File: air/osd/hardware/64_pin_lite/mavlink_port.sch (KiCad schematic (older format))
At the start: 4 parts, among them P4 CONN_6, U6 SI8642

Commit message: osd first  no eror routing of pcb
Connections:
- net FC_FRSKY_RXI: no longer P4.1, U6.14 (B1)
- new net FC_FRSKY_TXO: P4.1, U6.14 (B1)
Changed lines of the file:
@@
-EESchema Schematic File Version 2  date Thu 27 Nov 2014 15:59:43 GMT
+EESchema Schematic File Version 2  date Sat 29 Nov 2014 10:43:44 GMT
 LIBS:power
 LIBS:device
@@
 Sheet 6 8
 Title ""
-Date "27 nov 2014"
+Date "29 nov 2014"
 Rev ""
 Comp ""
@@
 $EndComp
 Text Label 7100 3800 0    45   ~ 0
-FC_FRSKY_RXI
+FC_FRSKY_TXO
 Text Label 7100 3700 0    45   ~ 0
 FC_GND

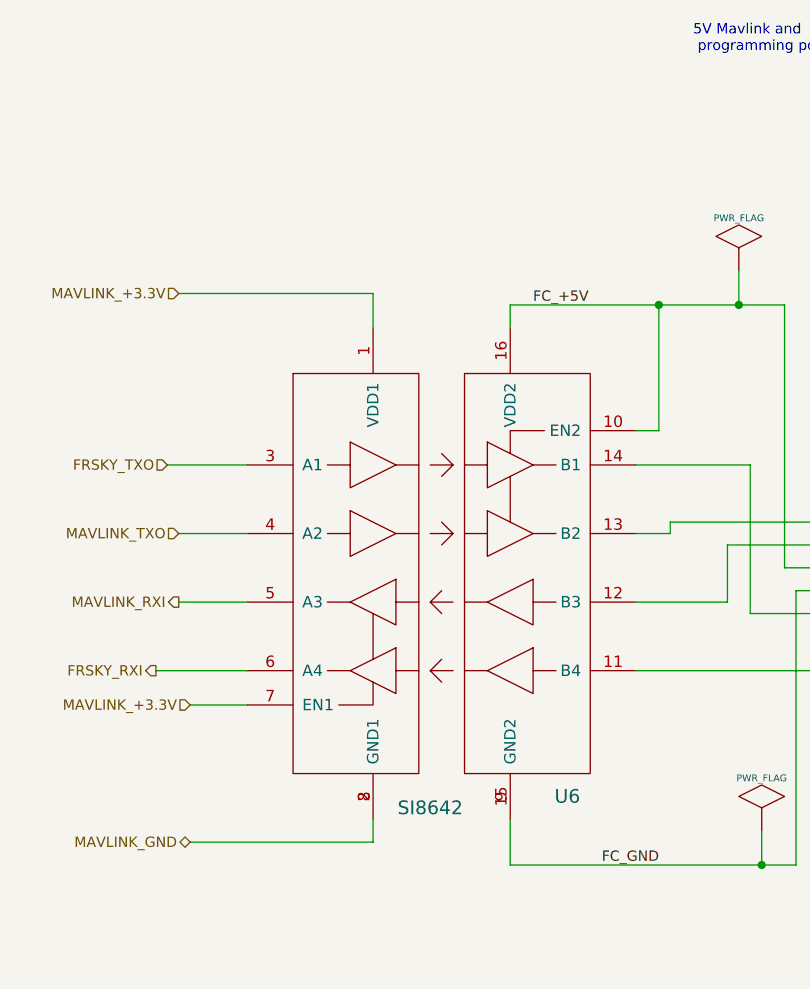
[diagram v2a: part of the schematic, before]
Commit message: added links for isolted port and other mods
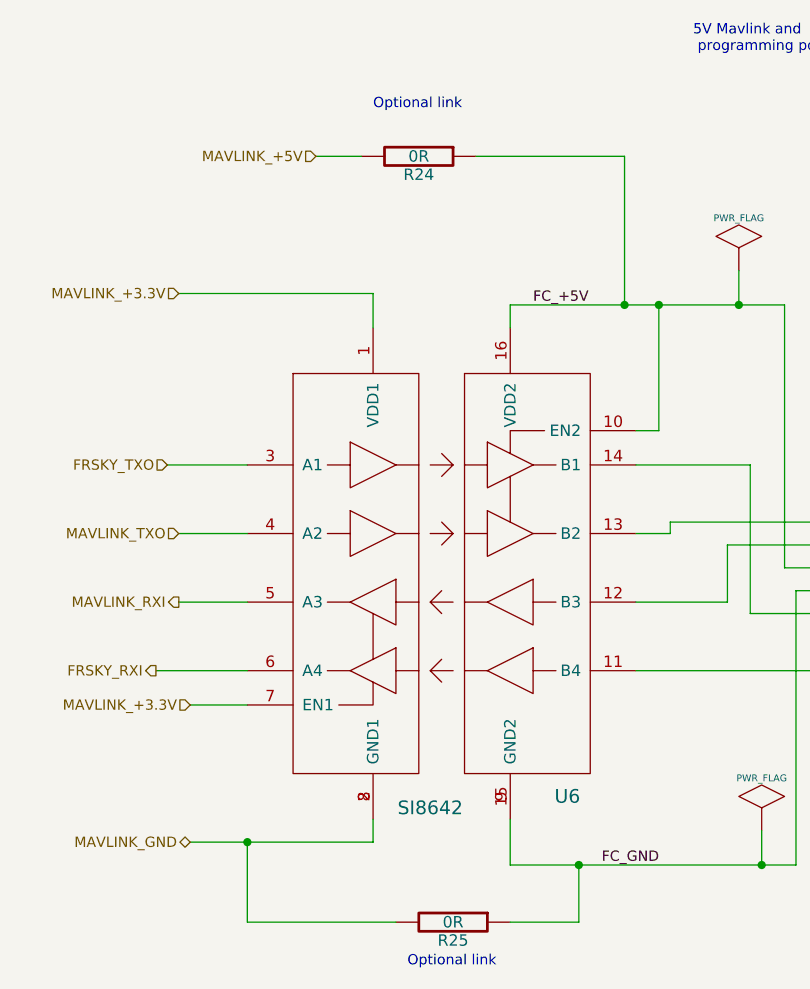
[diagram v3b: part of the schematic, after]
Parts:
- added R24, R25: 0R, symbol R
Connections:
- net FC_+5V: now also R24.1
- net FC_GND: now also R25.1
- net MAVLINK_GND: now also R25.2
- new net MAVLINK_+5V: R24.2
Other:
- note added: "Optional link"
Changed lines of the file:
@@
-EESchema Schematic File Version 2  date Sun 30 Nov 2014 15:34:12 GMT
+EESchema Schematic File Version 2  date Mon 01 Dec 2014 08:28:41 GMT
 LIBS:power
 LIBS:device
@@
 Sheet 6 8
 Title ""
-Date "30 nov 2014"
+Date "1 dec 2014"
 Rev ""
 Comp ""
@@
 Comment4 ""
 $EndDescr
+Text Notes 5100 1600 0    45   ~ 0
+Optional link
+Text Notes 5250 5350 0    45   ~ 0
+Optional link
+Connection ~ 4550 4800
+Wire Wire Line
+	4550 4800 4550 5150
+Wire Wire Line
+	4550 5150 5200 5150
+Connection ~ 6200 2450
+Wire Wire Line
+	6200 2450 6200 1800
+Wire Wire Line
+	6200 1800 5550 1800
 Wire Wire Line
 	2700 2800 2800 2800
@@
 Wire Wire Line
 	2800 2250 2800 2350
+Wire Wire Line
+	5050 1800 4850 1800
+Wire Wire Line
+	5700 5150 6000 5150
+Wire Wire Line
+	6000 5150 6000 4900
+Connection ~ 6000 4900
+$Comp
+L R R25
+U 1 1 547C2609
+P 5450 5150
+F 0 "R25" V 5530 5150 50  0000 C CNN
+F 1 "0R" V 5450 5150 50  0000 C CNN
+	1    5450 5150
+	0    1    1    0
+$EndComp
+$Comp
+L R R24
+U 1 1 547C2601
+P 5300 1800
+F 0 "R24" V 5380 1800 50  0000 C CNN
+F 1 "0R" V 5300 1800 50  0000 C CNN
+	1    5300 1800
+	0    1    1    0
+$EndComp
+Text HLabel 4850 1800 0    45   Input ~ 0
+MAVLINK_+5V
 Text HLabel 2700 2800 0    45   BiDi ~ 0
 MAVLINK_GND
@@
 FC_GND
 $Comp
-L PWR_FLAG #FLG05
+L PWR_FLAG #FLG6
 U 1 1 547339AD
 P 6800 4750
-F 0 "#FLG05" H 6800 5020 30  0001 C CNN
+F 0 "#FLG6" H 6800 5020 30  0001 C CNN
 F 1 "PWR_FLAG" H 6800 4980 30  0000 C CNN
 	1    6800 4750
@@
 $EndComp
 $Comp
-L PWR_FLAG #FLG06
+L PWR_FLAG #FLG5
 U 1 1 547339A4
 P 6700 2300
-F 0 "#FLG06" H 6700 2570 30  0001 C CNN
+F 0 "#FLG5" H 6700 2570 30  0001 C CNN
 F 1 "PWR_FLAG" H 6700 2530 30  0000 C CNN
 	1    6700 2300

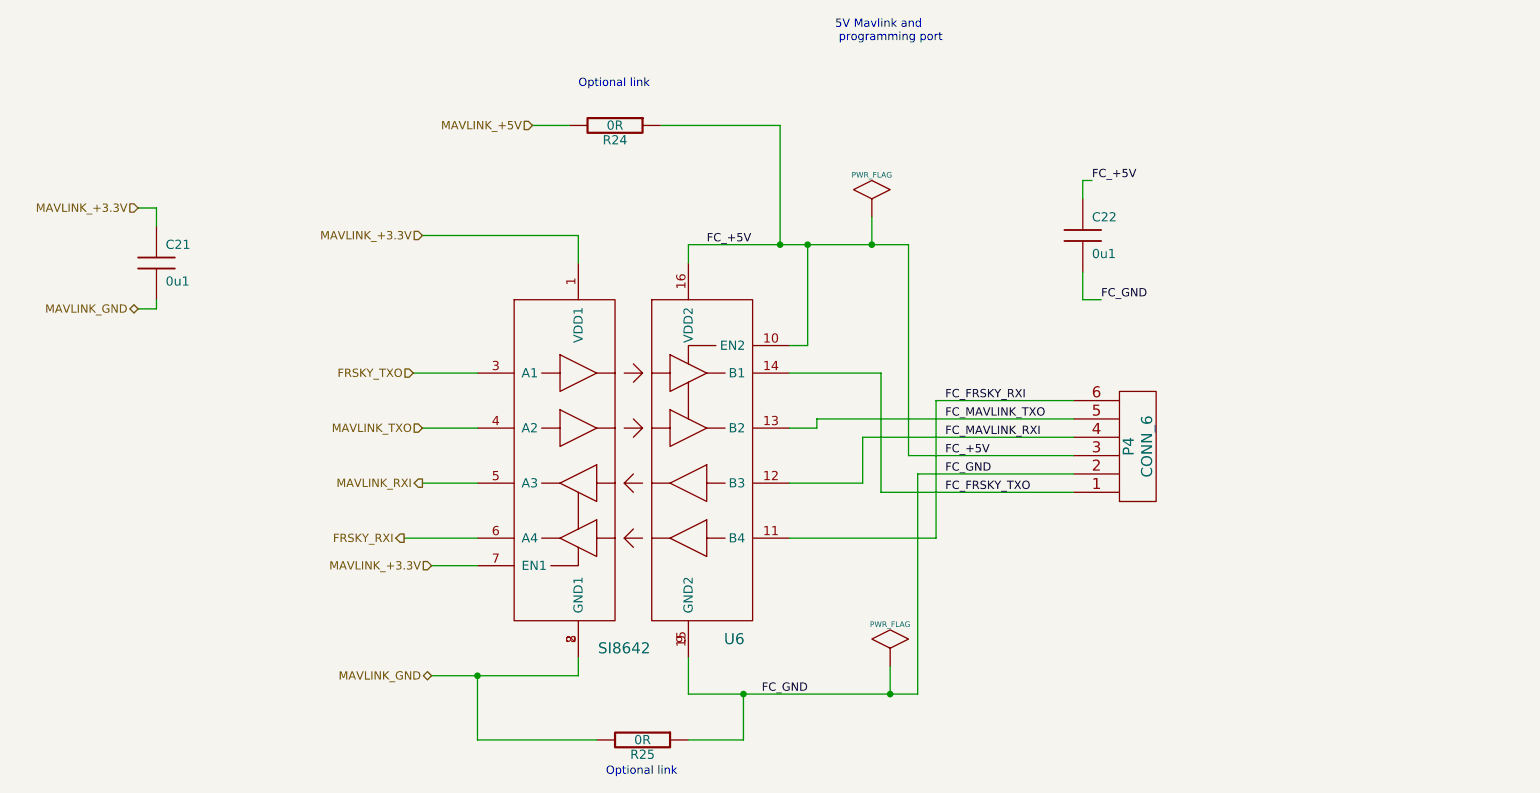
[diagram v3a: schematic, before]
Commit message: added resistors to output port on board and satrted on boardtype 4 port but currently in transition
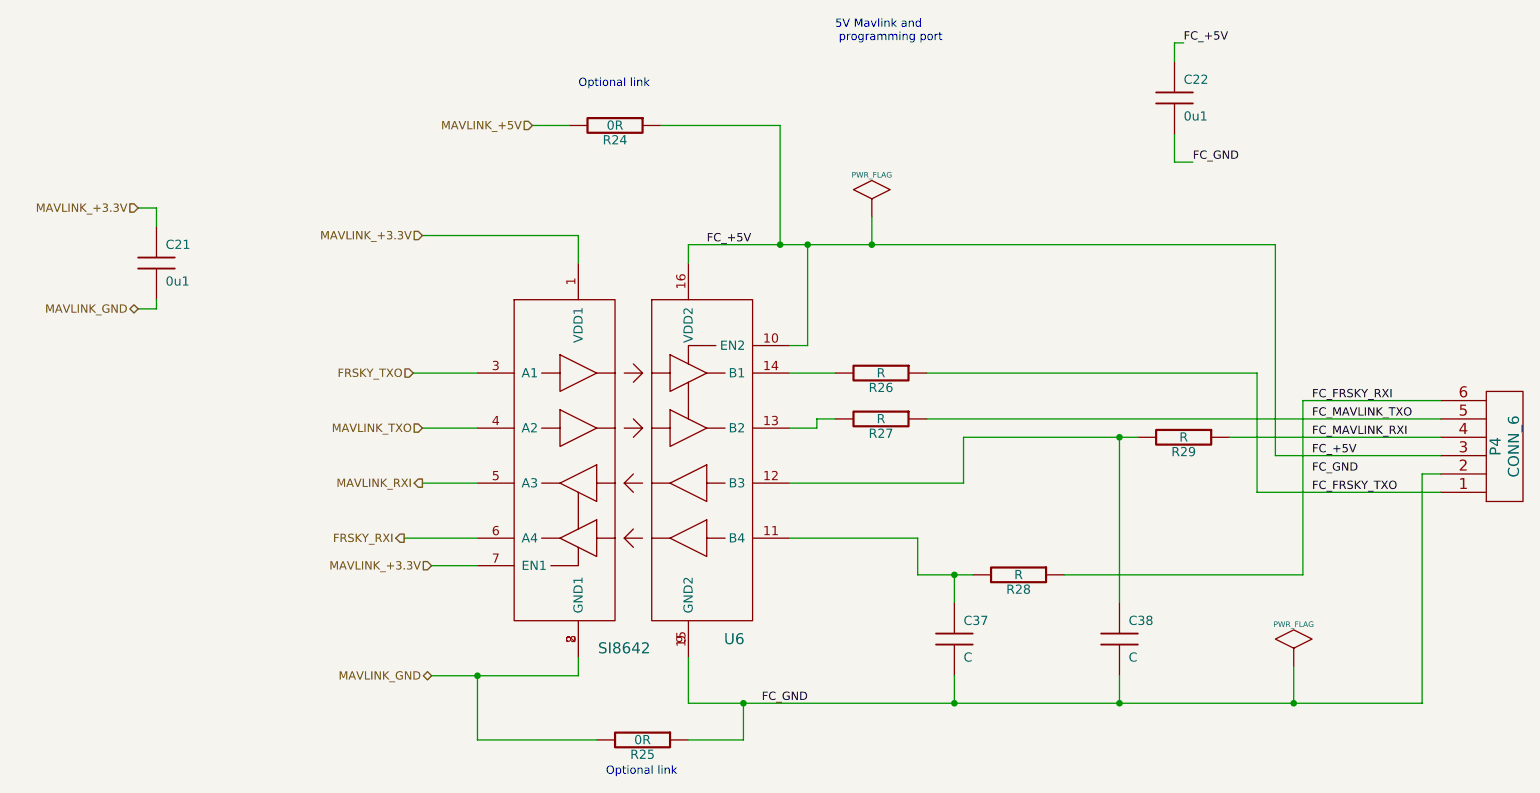
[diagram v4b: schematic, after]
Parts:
- added C37, C38: C, symbol C
- added R26, R27, R28, R29: R, symbol R
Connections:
- net FC_FRSKY_RXI: now also R28.1; no longer U6.11 (B4)
- net FC_FRSKY_TXO: now also R26.1; no longer U6.14 (B1)
- net FC_GND: now also C37.2, C38.2
- net FC_MAVLINK_RXI: now also R29.1; no longer U6.12 (B3)
- net FC_MAVLINK_TXO: now also R27.1; no longer U6.13 (B2)
- new net: C37.1, R28.2, U6.11 (B4)
- new net: C38.1, R29.2, U6.12 (B3)
- new net: R27.2, U6.13 (B2)
- new net: R26.2, U6.14 (B1)
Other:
- moved on the sheet: C22, P4
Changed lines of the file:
@@
-EESchema Schematic File Version 2  date Mon 01 Dec 2014 08:28:41 GMT
+EESchema Schematic File Version 2  date Tue 02 Dec 2014 12:33:05 GMT
 LIBS:power
 LIBS:device
@@
 Sheet 6 8
 Title ""
-Date "1 dec 2014"
+Date "2 dec 2014"
 Rev ""
 Comp ""
@@
 Comment4 ""
 $EndDescr
+Connection ~ 7150 4950
+Wire Wire Line
+	7150 4950 7150 4800
+Connection ~ 8050 3500
+Wire Wire Line
+	8050 4400 8050 3500
+Connection ~ 4550 4800
+Wire Wire Line
+	4550 4800 4550 5150
+Wire Wire Line
+	4550 5150 5200 5150
+Connection ~ 6200 2450
+Wire Wire Line
+	6200 2450 6200 1800
+Wire Wire Line
+	6200 1800 5550 1800
+Wire Wire Line
+	2700 2800 2800 2800
+Wire Wire Line
+	2800 2800 2800 2750
+Wire Wire Line
+	8350 1850 8350 2000
+Wire Wire Line
+	8350 2000 8450 2000
+Wire Wire Line
+	4550 4050 4150 4050
+Wire Wire Line
+	5100 4700 5100 4800
+Wire Wire Line
+	5100 4800 4300 4800
+Connection ~ 9000 4950
+Wire Wire Line
+	9000 4750 9000 4950
+Wire Wire Line
+	4550 3750 4250 3750
+Wire Wire Line
+	4550 3150 4200 3150
+Wire Wire Line
+	9050 3300 9050 4250
+Wire Wire Line
+	9050 3300 9800 3300
+Wire Wire Line
+	7250 4250 6950 4250
+Wire Wire Line
+	6950 4250 6950 4050
+Wire Wire Line
+	6950 4050 6250 4050
+Wire Wire Line
+	9050 4250 7750 4250
+Wire Wire Line
+	7000 3150 8800 3150
+Wire Wire Line
+	6250 3150 6500 3150
+Wire Wire Line
+	5100 2550 5100 2400
+Wire Wire Line
+	5100 2400 4250 2400
+Wire Wire Line
+	9800 3700 9700 3700
+Wire Wire Line
+	9700 3700 9700 4950
+Wire Wire Line
+	9700 4950 5700 4950
+Wire Wire Line
+	5700 4950 5700 4700
+Wire Wire Line
+	5700 2550 5700 2450
+Wire Wire Line
+	5700 2450 8900 2450
+Wire Wire Line
+	8900 2450 8900 3600
+Wire Wire Line
+	8900 3600 9800 3600
+Wire Wire Line
+	6250 3000 6350 3000
+Wire Wire Line
+	6350 3000 6350 2450
+Connection ~ 6350 2450
+Wire Wire Line
+	4550 4200 4300 4200
+Wire Wire Line
+	8150 3500 7200 3500
+Wire Wire Line
+	9800 3500 8650 3500
+Wire Wire Line
+	7200 3500 7200 3750
+Wire Wire Line
+	7200 3750 6250 3750
+Wire Wire Line
+	6500 3400 6400 3400
+Wire Wire Line
+	9800 3400 7000 3400
+Wire Wire Line
+	6400 3400 6400 3450
+Wire Wire Line
+	6400 3450 6250 3450
+Wire Wire Line
+	9800 3800 8800 3800
+Wire Wire Line
+	8800 3800 8800 3150
+Wire Wire Line
+	4550 3450 4250 3450
+Wire Wire Line
+	6700 2300 6700 2450
+Connection ~ 6700 2450
+Wire Wire Line
+	8350 1450 8350 1350
+Wire Wire Line
+	8350 1350 8400 1350
+Wire Wire Line
+	2700 2250 2800 2250
+Wire Wire Line
+	2800 2250 2800 2350
+Wire Wire Line
+	5050 1800 4850 1800
+Wire Wire Line
+	5700 5150 6000 5150
+Wire Wire Line
+	6000 5150 6000 4950
+Connection ~ 6000 4950
+Wire Wire Line
+	8050 4800 8050 4950
+Connection ~ 8050 4950
+Wire Wire Line
+	7150 4400 7150 4250
+Connection ~ 7150 4250
+$Comp
+L C C37
+U 1 1 547D825F
+P 7150 4600
+F 0 "C37" H 7200 4700 50  0000 L CNN
+F 1 "C" H 7200 4500 50  0000 L CNN
+	1    7150 4600
+	1    0    0    -1
+$EndComp
+$Comp
+L C C38
+U 1 1 547D8257
+P 8050 4600
+F 0 "C38" H 8100 4700 50  0000 L CNN
+F 1 "C" H 8100 4500 50  0000 L CNN
+	1    8050 4600
+	1    0    0    -1
+$EndComp
+$Comp
+L R R29
+U 1 1 547D81DE
+P 8400 3500
+F 0 "R29" V 8480 3500 50  0000 C CNN
+F 1 "R" V 8400 3500 50  0000 C CNN
+	1    8400 3500
+	0    1    1    0
+$EndComp
+$Comp
+L R R28
+U 1 1 547D81C5
+P 7500 4250
+F 0 "R28" V 7580 4250 50  0000 C CNN
+F 1 "R" V 7500 4250 50  0000 C CNN
+	1    7500 4250
+	0    1    1    0
+$EndComp
+$Comp
+L R R27
+U 1 1 547D816E
+P 6750 3400
+F 0 "R27" V 6830 3400 50  0000 C CNN
+F 1 "R" V 6750 3400 50  0000 C CNN
+	1    6750 3400
+	0    1    1    0
+$EndComp
+$Comp
+L R R26
+U 1 1 547D813B
+P 6750 3150
+F 0 "R26" V 6830 3150 50  0000 C CNN
+F 1 "R" V 6750 3150 50  0000 C CNN
+	1    6750 3150
+	0    1    1    0
+$EndComp
 Text Notes 5100 1600 0    45   ~ 0
 Optional link
 Text Notes 5250 5350 0    45   ~ 0
 Optional link
-Connection ~ 4550 4800
-Wire Wire Line
-	4550 4800 4550 5150
-Wire Wire Line
-	4550 5150 5200 5150
-Connection ~ 6200 2450
-Wire Wire Line
-	6200 2450 6200 1800
-Wire Wire Line
-	6200 1800 5550 1800
-Wire Wire Line
-	2700 2800 2800 2800
-Wire Wire Line
-	2800 2800 2800 2750
-Wire Wire Line
-	7850 2600 7850 2750
-Wire Wire Line
-	7850 2750 7950 2750
-Wire Wire Line
-	4550 4050 4150 4050
-Wire Wire Line
-	5100 4700 5100 4800
-Wire Wire Line
-	5100 4800 4300 4800
-Connection ~ 6800 4900
-Wire Wire Line
-	6800 4750 6800 4900
-Wire Wire Line
-	4550 3750 4250 3750
-Wire Wire Line
-	4550 3150 4200 3150
-Wire Wire Line
-	7050 3300 7050 4050
-Wire Wire Line
-	7050 3300 7800 3300
-Wire Wire Line
-	7050 4050 6250 4050
-Wire Wire Line
-	6250 3150 6750 3150
-Wire Wire Line
-	5100 2550 5100 2400
-Wire Wire Line
-	5100 2400 4250 2400
-Wire Wire Line
-	7800 3700 6950 3700
-Wire Wire Line
-	6950 3700 6950 4900
-Wire Wire Line
-	6950 4900 5700 4900
-Wire Wire Line
-	5700 4900 5700 4700
-Wire Wire Line
-	5700 2550 5700 2450
-Wire Wire Line
-	5700 2450 6900 2450
-Wire Wire Line
-	6900 2450 6900 3600
-Wire Wire Line
-	6900 3600 7800 3600
-Wire Wire Line
-	6250 3000 6350 3000
-Wire Wire Line
-	6350 3000 6350 2450
-Connection ~ 6350 2450
-Wire Wire Line
-	4550 4200 4300 4200
-Wire Wire Line
-	7800 3500 6650 3500
-Wire Wire Line
-	6650 3500 6650 3750
-Wire Wire Line
-	6650 3750 6250 3750
-Wire Wire Line
-	7800 3400 6400 3400
-Wire Wire Line
-	6400 3400 6400 3450
-Wire Wire Line
-	6400 3450 6250 3450
-Wire Wire Line
-	7800 3800 6750 3800
-Wire Wire Line
-	6750 3800 6750 3150
-Wire Wire Line
-	4550 3450 4250 3450
-Wire Wire Line
-	6700 2300 6700 2450
-Connection ~ 6700 2450
-Wire Wire Line
-	7850 2200 7850 2100
-Wire Wire Line
-	7850 2100 7900 2100
-Wire Wire Line
-	2700 2250 2800 2250
-Wire Wire Line
-	2800 2250 2800 2350
-Wire Wire Line
-	5050 1800 4850 1800
-Wire Wire Line
-	5700 5150 6000 5150
-Wire Wire Line
-	6000 5150 6000 4900
-Connection ~ 6000 4900
 $Comp
 L R R25
@@
 Text HLabel 2700 2250 0    45   Input ~ 0
 MAVLINK_+3.3V
-Text Label 7950 2750 0    45   ~ 0
+Text Label 8450 2000 0    45   ~ 0
 FC_GND
-Text Label 7900 2100 0    45   ~ 0
+Text Label 8400 1350 0    45   ~ 0
 FC_+5V
 $Comp
 L C C22
 U 1 1 54734555
-P 7850 2400
-F 0 "C22" H 7900 2500 50  0000 L CNN
-F 1 "0u1" H 7900 2300 50  0000 L CNN
-	1    7850 2400
+P 8350 1650
+F 0 "C22" H 8400 1750 50  0000 L CNN
+F 1 "0u1" H 8400 1550 50  0000 L CNN
+	1    8350 1650
 	1    0    0    -1
 $EndComp
@@
 	1    0    0    -1
 $EndComp
-Text Label 7100 3800 0    45   ~ 0
+Text Label 9100 3800 0    45   ~ 0
 FC_FRSKY_TXO
-Text Label 7100 3700 0    45   ~ 0
+Text Label 9100 3700 0    45   ~ 0
 FC_GND
-Text Label 7100 3600 0    45   ~ 0
+Text Label 9100 3600 0    45   ~ 0
 FC_+5V
-Text Label 7100 3500 0    45   ~ 0
+Text Label 9100 3500 0    45   ~ 0
 FC_MAVLINK_RXI
-Text Label 7100 3400 0    45   ~ 0
+Text Label 9100 3400 0    45   ~ 0
 FC_MAVLINK_TXO
-Text Label 7100 3300 0    45   ~ 0
+Text Label 9100 3300 0    45   ~ 0
 FC_FRSKY_RXI
-Text Label 6100 4900 0    45   ~ 0
+Text Label 6100 4950 0    45   ~ 0
 FC_GND
 $Comp
-L PWR_FLAG #FLG6
+L PWR_FLAG #FLG05
 U 1 1 547339AD
-P 6800 4750
-F 0 "#FLG6" H 6800 5020 30  0001 C CNN
-F 1 "PWR_FLAG" H 6800 4980 30  0000 C CNN
-	1    6800 4750
-	1    0    0    -1
-$EndComp
-$Comp
-L PWR_FLAG #FLG5
+P 9000 4750
+F 0 "#FLG05" H 9000 5020 30  0001 C CNN
+F 1 "PWR_FLAG" H 9000 4980 30  0000 C CNN
+	1    9000 4750
+	1    0    0    -1
+$EndComp
+$Comp
+L PWR_FLAG #FLG06
 U 1 1 547339A4
 P 6700 2300
-F 0 "#FLG5" H 6700 2570 30  0001 C CNN
+F 0 "#FLG06" H 6700 2570 30  0001 C CNN
 F 1 "PWR_FLAG" H 6700 2530 30  0000 C CNN
 	1    6700 2300
@@
 L CONN_6 P4
 U 1 1 546C98A1
-P 8150 3550
-F 0 "P4" V 8100 3550 60  0000 C CNN
-F 1 "CONN_6" V 8200 3550 60  0000 C CNN
-	1    8150 3550
+P 10150 3550
+F 0 "P4" V 10100 3550 60  0000 C CNN
+F 1 "CONN_6" V 10200 3550 60  0000 C CNN
+	1    10150 3550
 	1    0    0    1
 $EndComp

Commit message: sasve before moving psu caps on osd
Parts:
- C37, C38: value C -> 470pF
- R26, R27, R28, R29: value R -> 100R
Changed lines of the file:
@@
-EESchema Schematic File Version 2  date Wed 03 Dec 2014 09:37:23 GMT
+EESchema Schematic File Version 2  date Sun 07 Dec 2014 14:25:55 GMT
 LIBS:power
 LIBS:device
@@
 Sheet 6 8
 Title ""
-Date "3 dec 2014"
+Date "7 dec 2014"
 Rev ""
 Comp ""
@@
 P 7150 4600
 F 0 "C37" H 7200 4700 50  0000 L CNN
-F 1 "C" H 7200 4500 50  0000 L CNN
+F 1 "470pF" H 7200 4500 50  0000 L CNN
 	1    7150 4600
 	1    0    0    -1
@@
 P 8050 4600
 F 0 "C38" H 8100 4700 50  0000 L CNN
-F 1 "C" H 8100 4500 50  0000 L CNN
+F 1 "470pF" H 8100 4500 50  0000 L CNN
 	1    8050 4600
 	1    0    0    -1
@@
 P 8400 3500
 F 0 "R29" V 8480 3500 50  0000 C CNN
-F 1 "R" V 8400 3500 50  0000 C CNN
+F 1 "100R" V 8400 3500 50  0000 C CNN
 	1    8400 3500
 	0    1    1    0
@@
 P 7500 4250
 F 0 "R28" V 7580 4250 50  0000 C CNN
-F 1 "R" V 7500 4250 50  0000 C CNN
+F 1 "100R" V 7500 4250 50  0000 C CNN
 	1    7500 4250
 	0    1    1    0
@@
 P 6750 3400
 F 0 "R27" V 6830 3400 50  0000 C CNN
-F 1 "R" V 6750 3400 50  0000 C CNN
+F 1 "100R" V 6750 3400 50  0000 C CNN
 	1    6750 3400
 	0    1    1    0
@@
 P 6750 3150
 F 0 "R26" V 6830 3150 50  0000 C CNN
-F 1 "R" V 6750 3150 50  0000 C CNN
+F 1 "100R" V 6750 3150 50  0000 C CNN
 	1    6750 3150
 	0    1    1    0
